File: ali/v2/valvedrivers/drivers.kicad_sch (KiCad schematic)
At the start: 24 parts, among them J10 Conn_01x02, J11 Conn_01x02, J12 Conn_01x02, J9 Conn_01x02, U6 IPS4140HQ, U7 PS2841-4B, U8 PS2841-4B

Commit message: Globally remove LCSC labels, update MPNs and IOCs, add +5V monitoring to DAQs, fix some footprints
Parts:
- J12: MANUFACTURER (none) -> Molex; MPN (none) -> 503159-0201
- R24, R25, R26, R27, R30, R31, R32, R33: MPN RC0603FR-0710KL -> RC0603FR-0710KL
- U7, U8: MPN PS2841-4A-AX -> PS2841-4B-F3-AX
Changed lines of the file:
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@@
 			)
 		)
-		(property "MPN" "PS2841-4A-AX"
+		(property "MPN" "PS2841-4B-F3-AX"
 			(at 93.98 82.55 0)
 			(hide yes)
@@
 				)
 			)
-		)
-		(pin "1"
 		)
 		(pin "3"
@@
 			)
 		)
-		(property "MPN" " RC0603FR-0710KL"
+		(property "MPN" "RC0603FR-0710KL"
 			(at 120.65 144.78 90)
 			(hide yes)
@@
 			)
 		)
-		(property "MPN" " RC0603FR-0710KL"
+		(property "MPN" "RC0603FR-0710KL"
 			(at 149.86 83.82 0)
 			(hide yes)
@@
 			)
 		)
-		(property "MPN" " RC0603FR-0710KL"
+		(property "MPN" "RC0603FR-0710KL"
 			(at 120.65 125.73 90)
 			(hide yes)
@@
 			)
 		)
-		(property "MPN" " RC0603FR-0710KL"
+		(property "MPN" "RC0603FR-0710KL"
 			(at 120.65 138.43 90)
 			(hide yes)
@@
 		)
 		(property "Description" "Generic connector, single row, 01x02, script generated (kicad-library-utils/schlib/autogen/connector/)"
+			(at 248.92 90.17 0)
+			(hide yes)
+			(show_name no)
+			(do_not_autoplace no)
+			(effects
+				(font
+					(size 1.27 1.27)
+				)
+			)
+		)
+		(property "MPN" "503159-0201"
+			(at 248.92 90.17 0)
+			(hide yes)
+			(show_name no)
+			(do_not_autoplace no)
+			(effects
+				(font
+					(size 1.27 1.27)
+				)
+			)
+		)
+		(property "MANUFACTURER" "Molex"
 			(at 248.92 90.17 0)
 			(hide yes)
@@
 			)
 		)
-		(property "MPN" " RC0603FR-0710KL"
+		(property "MPN" "RC0603FR-0710KL"
 			(at 158.75 83.82 0)
 			(hide yes)
@@
 			)
 		)
-		(property "MPN" "PS2841-4A-AX"
+		(property "MPN" "PS2841-4B-F3-AX"
 			(at 95.25 134.62 0)
 			(hide yes)
@@
 				)
 			)
-		)
-		(pin "1"
 		)
 		(pin "3"
@@
 			)
 		)
-		(property "MPN" " RC0603FR-0710KL"
+		(property "MPN" "RC0603FR-0710KL"
 			(at 132.08 83.82 0)
 			(hide yes)
@@
 			)
 		)
-		(property "MPN" " RC0603FR-0710KL"
+		(property "MPN" "RC0603FR-0710KL"
 			(at 120.65 132.08 90)
 			(hide yes)
@@
 			)
 		)
-		(property "MPN" " RC0603FR-0710KL"
+		(property "MPN" "RC0603FR-0710KL"
 			(at 140.97 83.82 0)
 			(hide yes)

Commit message: Add ignition port to valve driver board, set up CANBUS keepouts
Daniel please don't see this I am embarassed
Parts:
- renumbered J9 to J10, J10 to J11, J11 to J12, J12 to J13
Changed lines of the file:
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@@
 		(dnp no)
 		(fields_autoplaced yes)
-		(property "Reference" "#PWR063"
+		(property "Reference" "#PWR066"
 			(at 110.49 68.58 0)
 			(hide yes)
@@
 			(project "valvedrivers"
 				(path "/0eb5ae8a-84ea-4b7e-bec4-bb4e0217d666/874202e5-99bb-4171-bb05-149c597c3ffb"
-					(reference "#PWR081")
+					(reference "#PWR084")
 					(unit 1)
 				)
 				(path "/0eb5ae8a-84ea-4b7e-bec4-bb4e0217d666/8cc59f38-1699-44c2-acba-89190a5df7d8"
-					(reference "#PWR063")
+					(reference "#PWR066")
 					(unit 1)
 				)
 				(path "/0eb5ae8a-84ea-4b7e-bec4-bb4e0217d666/9e5320c8-5979-4a17-b544-4eb9faf12b80"
-					(reference "#PWR072")
+					(reference "#PWR075")
 					(unit 1)
 				)
@@
 		(dnp no)
 		(fields_autoplaced yes)
-		(property "Reference" "#PWR064"
+		(property "Reference" "#PWR067"
 			(at 132.08 96.52 0)
 			(hide yes)
@@
 			(project "valvedrivers"
 				(path "/0eb5ae8a-84ea-4b7e-bec4-bb4e0217d666/874202e5-99bb-4171-bb05-149c597c3ffb"
-					(reference "#PWR082")
+					(reference "#PWR085")
 					(unit 1)
 				)
 				(path "/0eb5ae8a-84ea-4b7e-bec4-bb4e0217d666/8cc59f38-1699-44c2-acba-89190a5df7d8"
-					(reference "#PWR064")
+					(reference "#PWR067")
 					(unit 1)
 				)
 				(path "/0eb5ae8a-84ea-4b7e-bec4-bb4e0217d666/9e5320c8-5979-4a17-b544-4eb9faf12b80"
-					(reference "#PWR073")
+					(reference "#PWR076")
 					(unit 1)
 				)
@@
 		(in_pos_files yes)
 		(dnp no)
-		(property "Reference" "J12"
+		(property "Reference" "J13"
 			(at 251.46 91.44 0)
 			(show_name no)
@@
 			(project "valvedrivers"
 				(path "/0eb5ae8a-84ea-4b7e-bec4-bb4e0217d666/874202e5-99bb-4171-bb05-149c597c3ffb"
-					(reference "J20")
+					(reference "J21")
 					(unit 1)
 				)
 				(path "/0eb5ae8a-84ea-4b7e-bec4-bb4e0217d666/8cc59f38-1699-44c2-acba-89190a5df7d8"
-					(reference "J12")
+					(reference "J13")
 					(unit 1)
 				)
 				(path "/0eb5ae8a-84ea-4b7e-bec4-bb4e0217d666/9e5320c8-5979-4a17-b544-4eb9faf12b80"
-					(reference "J16")
+					(reference "J17")
 					(unit 1)
 				)
@@
 		(dnp no)
 		(fields_autoplaced yes)
-		(property "Reference" "#PWR068"
+		(property "Reference" "#PWR071"
 			(at 217.17 110.49 0)
 			(hide yes)
@@
 			(project "valvedrivers"
 				(path "/0eb5ae8a-84ea-4b7e-bec4-bb4e0217d666/874202e5-99bb-4171-bb05-149c597c3ffb"
-					(reference "#PWR086")
+					(reference "#PWR089")
 					(unit 1)
 				)
 				(path "/0eb5ae8a-84ea-4b7e-bec4-bb4e0217d666/8cc59f38-1699-44c2-acba-89190a5df7d8"
-					(reference "#PWR068")
+					(reference "#PWR071")
 					(unit 1)
 				)
 				(path "/0eb5ae8a-84ea-4b7e-bec4-bb4e0217d666/9e5320c8-5979-4a17-b544-4eb9faf12b80"
-					(reference "#PWR077")
+					(reference "#PWR080")
 					(unit 1)
 				)
@@
 		(dnp no)
 		(fields_autoplaced yes)
-		(property "Reference" "#PWR067"
+		(property "Reference" "#PWR070"
 			(at 83.82 106.68 0)
 			(hide yes)
@@
 			(project "valvedrivers"
 				(path "/0eb5ae8a-84ea-4b7e-bec4-bb4e0217d666/874202e5-99bb-4171-bb05-149c597c3ffb"
-					(reference "#PWR085")
+					(reference "#PWR088")
 					(unit 1)
 				)
 				(path "/0eb5ae8a-84ea-4b7e-bec4-bb4e0217d666/8cc59f38-1699-44c2-acba-89190a5df7d8"
-					(reference "#PWR067")
+					(reference "#PWR070")
 					(unit 1)
 				)
 				(path "/0eb5ae8a-84ea-4b7e-bec4-bb4e0217d666/9e5320c8-5979-4a17-b544-4eb9faf12b80"
-					(reference "#PWR076")
+					(reference "#PWR079")
 					(unit 1)
 				)
@@
 		(in_pos_files yes)
 		(dnp no)
-		(property "Reference" "J11"
+		(property "Reference" "J12"
 			(at 251.46 83.82 0)
 			(show_name no)
@@
 			(project "valvedrivers"
 				(path "/0eb5ae8a-84ea-4b7e-bec4-bb4e0217d666/874202e5-99bb-4171-bb05-149c597c3ffb"
-					(reference "J19")
+					(reference "J20")
 					(unit 1)
 				)
 				(path "/0eb5ae8a-84ea-4b7e-bec4-bb4e0217d666/8cc59f38-1699-44c2-acba-89190a5df7d8"
-					(reference "J11")
+					(reference "J12")
 					(unit 1)
 				)
 				(path "/0eb5ae8a-84ea-4b7e-bec4-bb4e0217d666/9e5320c8-5979-4a17-b544-4eb9faf12b80"
-					(reference "J15")
+					(reference "J16")
 					(unit 1)
 				)
@@
 		(dnp no)
 		(fields_autoplaced yes)
-		(property "Reference" "#PWR061"
+		(property "Reference" "#PWR064"
 			(at 196.85 50.8 0)
 			(hide yes)
@@
 			(project "valvedrivers"
 				(path "/0eb5ae8a-84ea-4b7e-bec4-bb4e0217d666/874202e5-99bb-4171-bb05-149c597c3ffb"
-					(reference "#PWR079")
+					(reference "#PWR082")
 					(unit 1)
 				)
 				(path "/0eb5ae8a-84ea-4b7e-bec4-bb4e0217d666/8cc59f38-1699-44c2-acba-89190a5df7d8"
-					(reference "#PWR061")
+					(reference "#PWR064")
 					(unit 1)
 				)
 				(path "/0eb5ae8a-84ea-4b7e-bec4-bb4e0217d666/9e5320c8-5979-4a17-b544-4eb9faf12b80"
-					(reference "#PWR070")
+					(reference "#PWR073")
 					(unit 1)
 				)
@@
 		(dnp no)
 		(fields_autoplaced yes)
-		(property "Reference" "#PWR066"
+		(property "Reference" "#PWR069"
 			(at 196.85 104.14 0)
 			(hide yes)
@@
 			(project "valvedrivers"
 				(path "/0eb5ae8a-84ea-4b7e-bec4-bb4e0217d666/874202e5-99bb-4171-bb05-149c597c3ffb"
-					(reference "#PWR084")
+					(reference "#PWR087")
 					(unit 1)
 				)
 				(path "/0eb5ae8a-84ea-4b7e-bec4-bb4e0217d666/8cc59f38-1699-44c2-acba-89190a5df7d8"
-					(reference "#PWR066")
+					(reference "#PWR069")
 					(unit 1)
 				)
 				(path "/0eb5ae8a-84ea-4b7e-bec4-bb4e0217d666/9e5320c8-5979-4a17-b544-4eb9faf12b80"
-					(reference "#PWR075")
+					(reference "#PWR078")
 					(unit 1)
 				)
@@
 		(dnp no)
 		(fields_autoplaced yes)
-		(property "Reference" "#PWR065"
+		(property "Reference" "#PWR068"
 			(at 240.03 97.79 0)
 			(hide yes)
@@
 			(project "valvedrivers"
 				(path "/0eb5ae8a-84ea-4b7e-bec4-bb4e0217d666/874202e5-99bb-4171-bb05-149c597c3ffb"
-					(reference "#PWR083")
+					(reference "#PWR086")
 					(unit 1)
 				)
 				(path "/0eb5ae8a-84ea-4b7e-bec4-bb4e0217d666/8cc59f38-1699-44c2-acba-89190a5df7d8"
-					(reference "#PWR065")
+					(reference "#PWR068")
 					(unit 1)
 				)
 				(path "/0eb5ae8a-84ea-4b7e-bec4-bb4e0217d666/9e5320c8-5979-4a17-b544-4eb9faf12b80"
-					(reference "#PWR074")
+					(reference "#PWR077")
 					(unit 1)
 				)
@@
 		(dnp no)
 		(fields_autoplaced yes)
-		(property "Reference" "#PWR062"
+		(property "Reference" "#PWR065"
 			(at 184.15 63.5 0)
 			(hide yes)
@@
 			(project "valvedrivers"
 				(path "/0eb5ae8a-84ea-4b7e-bec4-bb4e0217d666/874202e5-99bb-4171-bb05-149c597c3ffb"
-					(reference "#PWR080")
+					(reference "#PWR083")
 					(unit 1)
 				)
 				(path "/0eb5ae8a-84ea-4b7e-bec4-bb4e0217d666/8cc59f38-1699-44c2-acba-89190a5df7d8"
-					(reference "#PWR062")
+					(reference "#PWR065")
 					(unit 1)
 				)
 				(path "/0eb5ae8a-84ea-4b7e-bec4-bb4e0217d666/9e5320c8-5979-4a17-b544-4eb9faf12b80"
-					(reference "#PWR071")
+					(reference "#PWR074")
 					(unit 1)
 				)
@@
 		(dnp no)
 		(fields_autoplaced yes)
-		(property "Reference" "#PWR069"
+		(property "Reference" "#PWR072"
 			(at 71.12 118.11 0)
 			(hide yes)
@@
 			(project "valvedrivers"
 				(path "/0eb5ae8a-84ea-4b7e-bec4-bb4e0217d666/874202e5-99bb-4171-bb05-149c597c3ffb"
-					(reference "#PWR087")
+					(reference "#PWR090")
 					(unit 1)
 				)
 				(path "/0eb5ae8a-84ea-4b7e-bec4-bb4e0217d666/8cc59f38-1699-44c2-acba-89190a5df7d8"
-					(reference "#PWR069")
+					(reference "#PWR072")
 					(unit 1)
 				)
 				(path "/0eb5ae8a-84ea-4b7e-bec4-bb4e0217d666/9e5320c8-5979-4a17-b544-4eb9faf12b80"
-					(reference "#PWR078")
+					(reference "#PWR081")
 					(unit 1)
 				)
@@
 		(in_pos_files yes)
 		(dnp no)
-		(property "Reference" "J9"
+		(property "Reference" "J10"
 			(at 251.46 68.58 0)
 			(show_name no)
@@
 			(project "valvedrivers"
 				(path "/0eb5ae8a-84ea-4b7e-bec4-bb4e0217d666/874202e5-99bb-4171-bb05-149c597c3ffb"
-					(reference "J17")
+					(reference "J18")
 					(unit 1)
 				)
 				(path "/0eb5ae8a-84ea-4b7e-bec4-bb4e0217d666/8cc59f38-1699-44c2-acba-89190a5df7d8"
-					(reference "J9")
+					(reference "J10")
 					(unit 1)
 				)
 				(path "/0eb5ae8a-84ea-4b7e-bec4-bb4e0217d666/9e5320c8-5979-4a17-b544-4eb9faf12b80"
-					(reference "J13")
+					(reference "J14")
 					(unit 1)
 				)
@@
 		(in_pos_files yes)
 		(dnp no)
-		(property "Reference" "J10"
+		(property "Reference" "J11"
 			(at 251.46 76.2 0)
 			(show_name no)
@@
 			(project "valvedrivers"
 				(path "/0eb5ae8a-84ea-4b7e-bec4-bb4e0217d666/874202e5-99bb-4171-bb05-149c597c3ffb"
-					(reference "J18")
+					(reference "J19")
 					(unit 1)
 				)
 				(path "/0eb5ae8a-84ea-4b7e-bec4-bb4e0217d666/8cc59f38-1699-44c2-acba-89190a5df7d8"
-					(reference "J10")
+					(reference "J11")
 					(unit 1)
 				)
 				(path "/0eb5ae8a-84ea-4b7e-bec4-bb4e0217d666/9e5320c8-5979-4a17-b544-4eb9faf12b80"
-					(reference "J14")
-					(unit 1)
-				)
+					(reference "J15")
+					(unit 1)
+				)

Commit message: Commentary
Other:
- note added: "DRIVER"
- note added: "I'm still not sold on this "bus switch" concept. Like if we lose +3.3V all the outputs are going low anyway, and here I'm not even offering the option to jumper things. Nobody does a "safe default" state where some outputs are high because what, if the board loses power the system is unsafe?"
- note added: "OPTOCOUPLER"
- note added: "not sure about this diode choice"
- moved on the sheet: C29, D10, D11, D8, D9, J10, J11, J12, J13, R22, R23, R24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

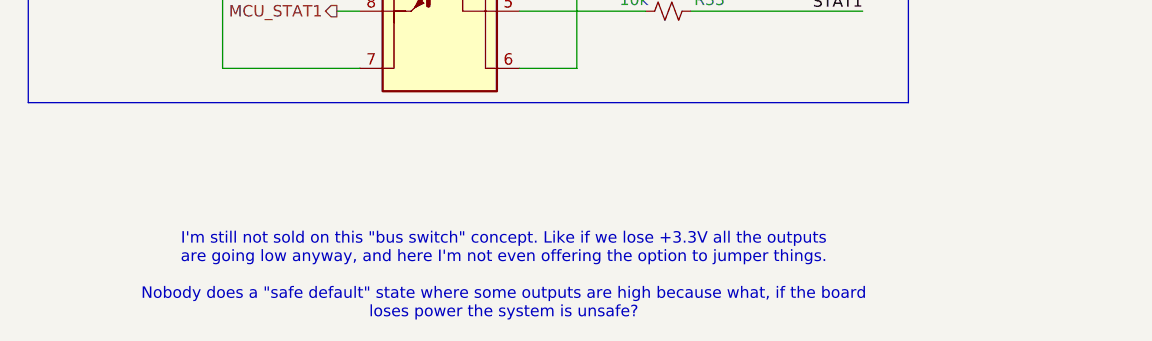
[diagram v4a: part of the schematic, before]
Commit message: Document setup, update template, and use an ampersand when referring to APRL
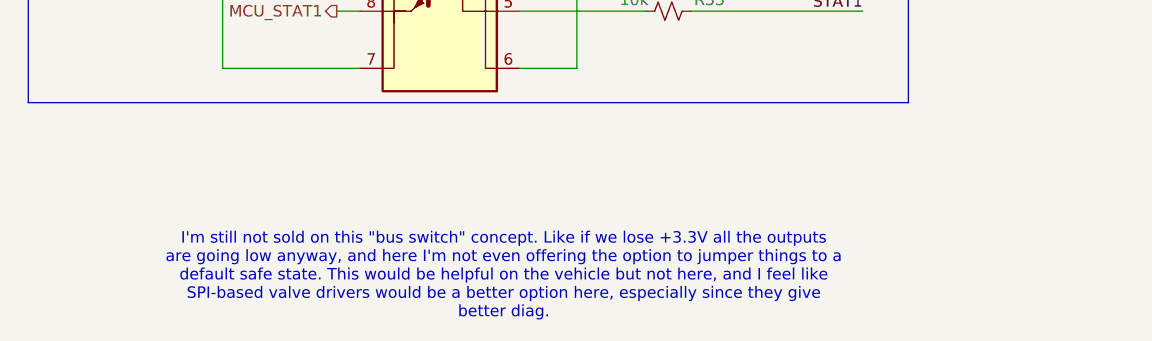
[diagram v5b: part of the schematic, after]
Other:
- note added: "I'm still not sold on this "bus switch" concept. Like if we lose +3.3V all the outputs are going low anyway, and here I'm not even offering the option to jumper things to a default safe state. This would be helpful on the vehicle but not here, and I feel like SPI-based valve drivers would be a better option here, especially since they give better diag."
- note removed: "I'm still not sold on this "bus switch" concept. Like if we lose +3.3V all the outputs are going low anyway, and here I'm not even offering the option to jumper things. Nobody does a "safe default" state where some outputs are high because what, if the board loses power the system is unsafe?"
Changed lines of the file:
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@@
 		)
 	)
-	(text "I'm still not sold on this \"bus switch\" concept. Like if we lose +3.3V all the outputs\nare going low anyway, and here I'm not even offering the option to jumper things.\n\nNobody does a \"safe default\" state where some outputs are high because what, if the board\nloses power the system is unsafe?"
+	(text "I'm still not sold on this \"bus switch\" concept. Like if we lose +3.3V all the outputs\nare going low anyway, and here I'm not even offering the option to jumper things to a\ndefault safe state. This would be helpful on the vehicle but not here, and I feel like\nSPI-based valve drivers would be a better option here, especially since they give\nbetter diag."
 		(exclude_from_sim no)
 		(at 75.692 171.704 0)

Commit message: Begin prep for second board review
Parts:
- removed D10, D11, D8, D9: SMF4L33CA, Diode_SMD:D_SOD-123F, symbol Device:D_TVS
- removed R22, R23: 1k, APRL_Passive:R_0603, symbol Device:R_Small_US
- removed U7, U8: PS2841-4B, APRL_Package:SOIC-12, symbol APRL_Power:PS2841-4B
- added C30, C31, C37: 100nF, APRL_Passive:C_0603, symbol Device:C_Small
- added C32, C33, C34, C35, C38, C39, C40, C41: 10nF, APRL_Passive:C_0603, symbol Device:C_Small
- added C36: 47uF, APRL_Passive:KEMET MU VIB, symbol Device:C_Polarized_Small_US
- added J10, J11, J12, J13: Conn_01x02, APRL_Connector_Molex:Molex_CLIK-Mate_503159-0201_1x02-1MP_P1.50mm_Vertical, symbol Connector_Generic:Conn_01x02
- added R24, R25, R26, R27, R34, R35: 10k, APRL_Passive:R_0603, symbol Device:R_Small_US
- added U7: SN74CBTLV3245A, APRL_Package:TSSOP-20_4.4x6.5mm_P0.65mm, symbol APRL_Analog:SN74CBTLV3245A
- added U8: IPS4140HQ, APRL_Package:QFN-48_EP_9.01x7.01_Pitch0.5mm, symbol APRL_Power:IPS4140HQ
- R28, R29: value 1k -> 10k; MPN RT0603BRD071KL -> RC0603FR-0710KL
- renumbered J10 to J14, J11 to J15, J12 to J16, J13 to J17, R24 to R36, R25 to R37, R26 to R38, R27 to R39, U6 to U9
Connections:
- net GNDPWR is gone; now on net GND: C29.2, J14.2 (Pin_2), J15.2 (Pin_2), J16.2 (Pin_2), J17.2 (Pin_2), R36.2, R37.2, R38.2, R39.2, U9.17 (GND)
- net +24V: now also C30.1, C36.1, C37.1, U8.49 (VCC)
- net +3.3V: now also R32.1, R33.1, C31.1, R24.1, R25.1, R26.1, R27.1, R34.1, R35.1, U7.20 (VCC)
- net GND: now also R28.2, R29.2, R30.2, R31.2, C30.2, C31.2, C32.2, C33.2, C34.2, C35.2, C36.2, C37.2, C38.2, C39.2, C40.2, C41.2, J10.2 (Pin_2), J11.2 (Pin_2), J12.2 (Pin_2), J13.2 (Pin_2), U7.10 (GND), U8.17 (GND)
- net MCU_IN1: now also U7.9 (A8); no longer R29.1
- net MCU_IN2: now also U7.8 (A7); no longer R28.1
- net MCU_IN3: now also U7.7 (A6)
- net MCU_IN4: now also U7.6 (A5)
- net MCU_STAT1: now also R24.2, U8.20 (STAT4)
- net MCU_STAT2: now also R25.2, U8.18 (STAT3)
- net MCU_STAT3: now also R26.2, U8.16 (STAT2)
- net MCU_STAT4: now also R27.2, U8.14 (STAT1)
- net at J14.1 (Pin_1), U9.36 (OUT4), U9.37 (OUT4)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: now also C38.1
- net at J15.1 (Pin_1), U9.39 (OUT3), U9.40 (OUT3)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: now also C39.1
- net at J16.1 (Pin_1), U9.42 (OUT2), U9.43 (OUT2)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: now also C40.1
- net at J17.1 (Pin_1), U9.45 (OUT1), U9.46 (OUT1)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: now also C41.1
- net at R30.1: now also U7.12 (B7), U8.19 (IN3)
- net at R31.1: now also U7.11 (B8), U8.21 (IN4)
- net IN1: no longer names the net of R36.1, U9.13 (IN1)
- net IN1: now also U7.18 (B1)
- net IN2: no longer names the net of R37.1, U9.15 (IN2)
- net IN2: now also U7.17 (B2)
- net IN3: no longer names the net of R38.1, U9.19 (IN3)
- net IN3: now also U7.16 (B3)
- net IN4: no longer names the net of R39.1, U9.21 (IN4)
- net IN4: now also U7.15 (B4)
- net STAT1 renamed MCU_STAT6
- net MCU_STAT6: now also U9.18 (STAT3); no longer U9.14 (STAT1)
- net STAT2 renamed MCU_STAT5
- net MCU_STAT5: now also U9.20 (STAT4); no longer U9.16 (STAT2)
- removed net STAT3: R31.2, U9.18 (STAT3)
- removed net STAT4: R30.2, U9.20 (STAT4)
- new net: R29.1, U7.13 (B6), U8.15 (IN2)
- new net: R28.1, U7.14 (B5), U8.13 (IN1)
- new net: C33.1, J11.1 (Pin_1), U8.39 (OUT3), U8.40 (OUT3), U8.41 (OUT3)
- new net: C32.1, J10.1 (Pin_1), U8.36 (OUT4), U8.37 (OUT4), U8.38 (OUT4)
- new net: C34.1, J12.1 (Pin_1), U8.42 (OUT2), U8.43 (OUT2), U8.44 (OUT2)
- new net: U8.1 (NC), U8.10 (NC), U8.11 (NC), U8.12 (NC), U8.2 (NC), U8.22 (NC), U8.23 (NC), U8.24 (NC), U8.25 (NC), U8.26 (NC), U8.27 (NC), U8.28 (NC), U8.29 (NC), U8.3 (NC), U8.30 (NC), U8.31 (NC), U8.32 (NC), U8.33 (NC), U8.34 (NC), U8.35 (NC), U8.4 (NC), U8.48 (NC), U8.5 (NC), U8.6 (NC), U8.7 (NC), U8.8 (NC), U8.9 (NC)
- new net: C35.1, J13.1 (Pin_1), U8.45 (OUT1), U8.46 (OUT1), U8.47 (OUT1)
- new net MCU_IN5: U7.5 (A4)
- new net MCU_IN6: U7.4 (A3)
- new net MCU_IN7: U7.3 (A2)
- new net MCU_IN8: U7.2 (A1)
- new net MCU_STAT7: R34.2, U9.16 (STAT2)
- new net MCU_STAT8: R35.2, U9.14 (STAT1)
- new net ~{BUSS_EN}: U7.19 (~{OE})
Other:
- note removed: "DRIVER"
- note removed: "I'm still not sold on this "bus switch" concept. Like if we lose +3.3V all the outputs are going low anyway, and here I'm not even offering the option to jumper things to a default safe state. This would be helpful on the vehicle but not here, and I feel like SPI-based valve drivers would be a better option here, especially since they give better diag."
- note removed: "OPTOCOUPLER"
- note removed: "Unidirectional not bidirectional as to not interfere with IPS4140HQ's active clamping"
- note removed: "We will be using internal pulldowns on STM32H5 side"
- note removed: "not sure about this diode choice"
- moved on the sheet: C29, J14, J15, J16, J17, R36, R37, R38, R39, U9
